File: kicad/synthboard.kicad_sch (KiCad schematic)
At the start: 11 parts, among them J1 Conn_02x20_Odd_Even, J2 Conn_02x20_Odd_Even, J3 Analog_Audio_Out, U1 MAX98357A

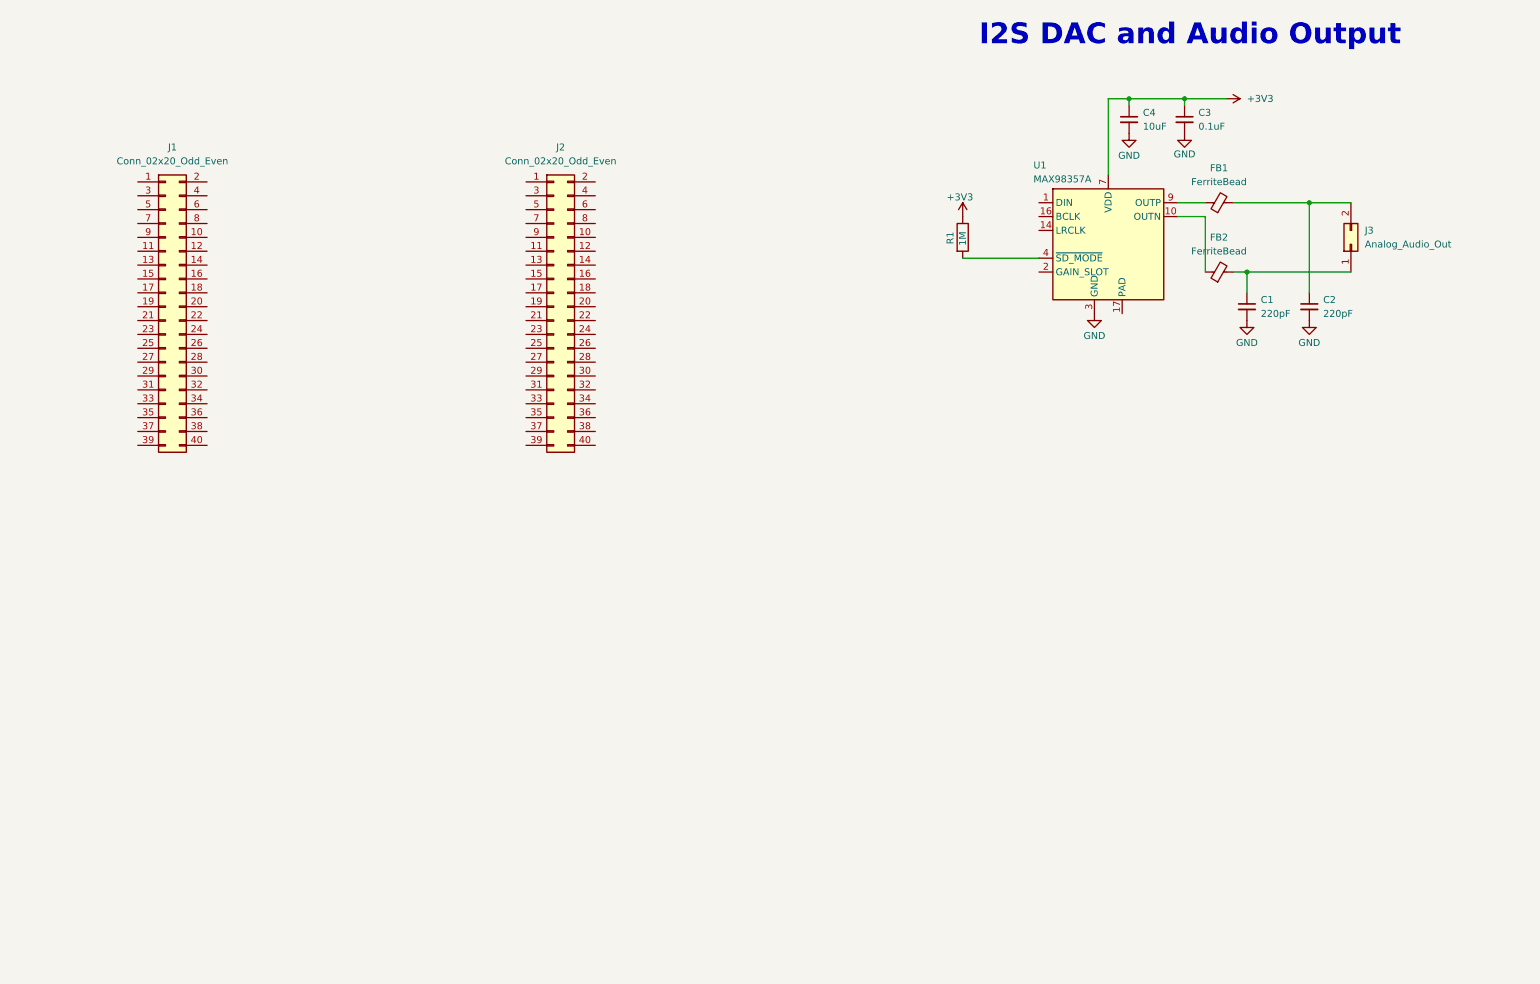
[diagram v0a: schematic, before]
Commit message: PCB development for input board started
Not done. Need to make a GND and +3.3V layer
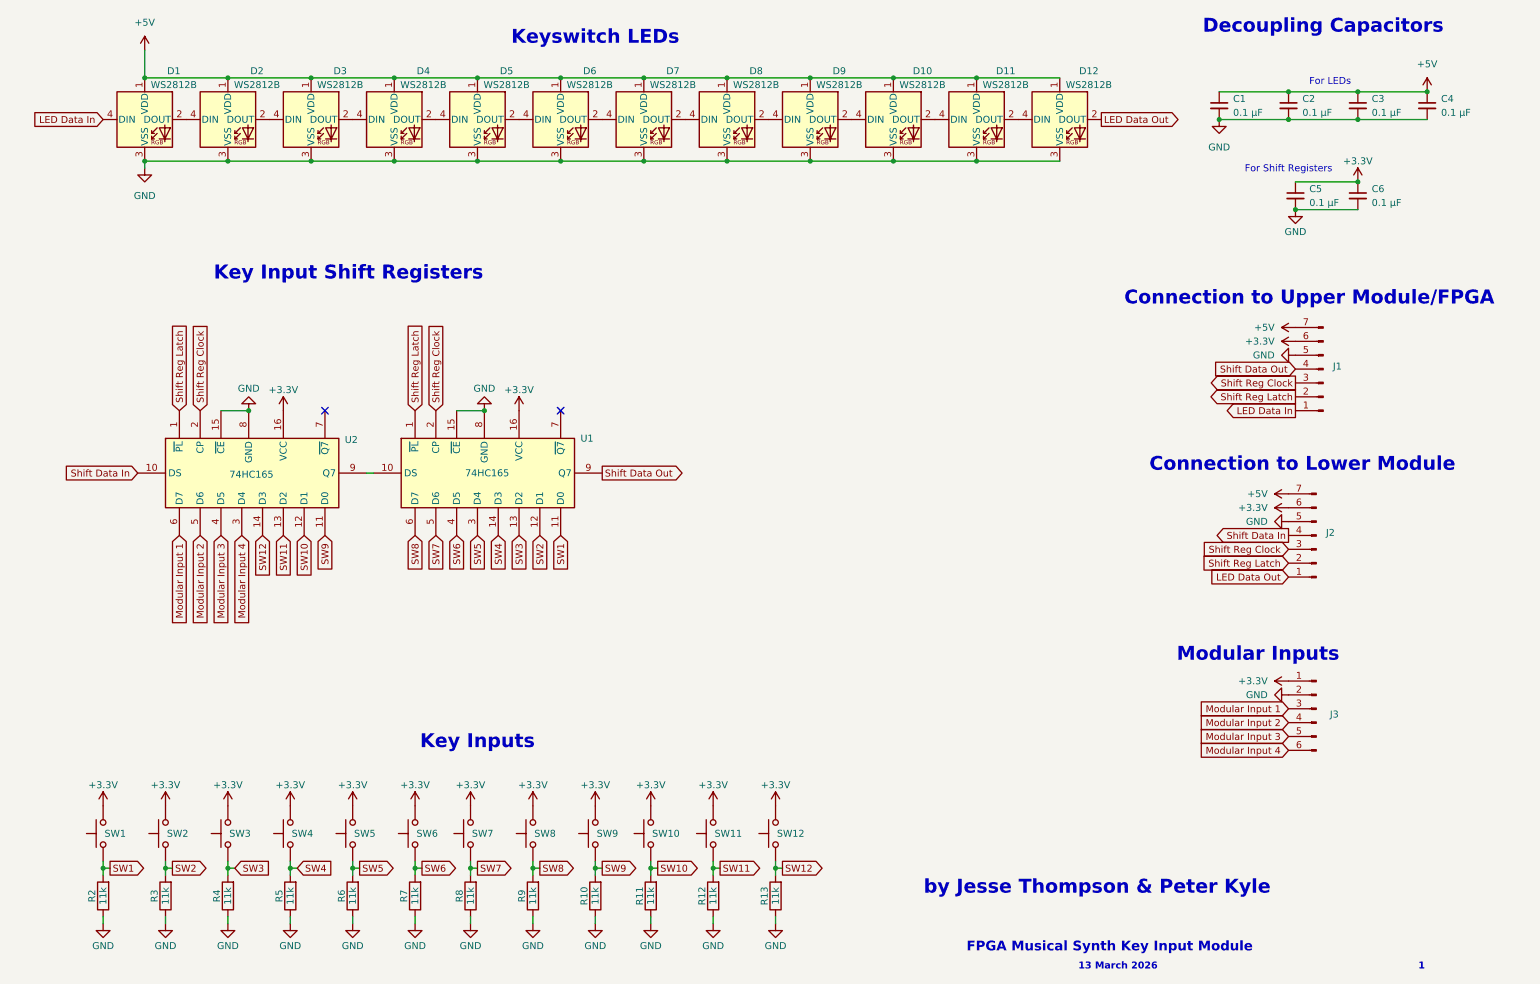
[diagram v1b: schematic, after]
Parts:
- removed FB1, FB2: FerriteBead, symbol Device:FerriteBead_Small
- removed J1, J2: Conn_02x20_Odd_Even, symbol Connector_Generic:Conn_02x20_Odd_Even
- removed J3: Analog_Audio_Out, symbol Connector_Generic:Conn_02x01
- removed R1: 1M, symbol Device:R
- removed U1: MAX98357A, Package_DFN_QFN:TQFN-16-1EP_3x3mm_P0.5mm_EP1.23x1.23mm, symbol Audio:MAX98357A
- added C5, C6: 0.1 µF, Capacitor_SMD:C_0805_2012Metric, symbol Device:C_Small
- added D1, D10, D11, D12, D2, D3, D4, D5, D6, D7, D8, D9: WS2812B, LED_SMD:LED_WS2812B_PLCC4_5.0x5.0mm_P3.2mm, symbol LED:WS2812B
- added J1: Connection to Upper Module/FPGA, Connector_PinHeader_2.54mm:PinHeader_1x07_P2.54mm_Vertical, symbol Connector:Conn_01x07_Pin
- added J2: Connection to Lower Module, Connector_PinHeader_2.54mm:PinHeader_1x07_P2.54mm_Vertical, symbol Connector:Conn_01x07_Pin
- added J3: Modular Inputs, Connector_PinHeader_2.54mm:PinHeader_1x06_P2.54mm_Vertical, symbol Connector:Conn_01x06_Pin
- added R10, R11, R12, R13, R2, R3, R4, R5, R6, R7, R8, R9: 11k, Resistor_SMD:R_0805_2012Metric, symbol Device:R
- added SW1, SW10, SW11, SW12, SW2, SW3, SW4, SW5, SW6, SW7, SW8, SW9: SW_Push, Button_Switch_Keyboard:SW_Cherry_MX_1.00u_Plate, symbol Switch:SW_Push
- added U1, U2: 74HC165, 74HC165D_653:SOIC127P600X175-16N, symbol 74xx:74HC165
- C1, C2: value 220pF -> 0.1 µF; footprint (none) -> Capacitor_SMD:C_0805_2012Metric
- C3: value 0.1uF -> 0.1 µF; footprint (none) -> Capacitor_SMD:C_0805_2012Metric
- C4: value 10uF -> 0.1 µF; footprint (none) -> Capacitor_SMD:C_0805_2012Metric
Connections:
- net +3V3 is gone; now on net +5V: C3.1, C4.1
- net GND: now also C5.2, C6.2, D1.3 (VSS), D10.3 (VSS), D11.3 (VSS), D12.3 (VSS), D2.3 (VSS), D3.3 (VSS), D4.3 (VSS), D5.3 (VSS), D6.3 (VSS), D7.3 (VSS), D8.3 (VSS), D9.3 (VSS), J1.5 (Pin_5), J2.5 (Pin_5), J3.2 (Pin_2), R10.1, R11.1, R12.1, R13.1, R2.1, R3.1, R4.1, R5.1, R6.1, R7.1, R8.1, R9.1, U1.15 (~{CE}), U1.8 (GND), U2.15 (~{CE}), U2.8 (GND)
- net +5V: now reaches C2.1
- net +5V: now also C1.1, D1.1 (VDD), D10.1 (VDD), D11.1 (VDD), D12.1 (VDD), D2.1 (VDD), D3.1 (VDD), D4.1 (VDD), D5.1 (VDD), D6.1 (VDD), D7.1 (VDD), D8.1 (VDD), D9.1 (VDD), J1.7 (Pin_7), J2.7 (Pin_7)
- new net: D10.2 (DOUT), D11.4 (DIN)
- new net: D10.4 (DIN), D9.2 (DOUT)
- new net: D11.2 (DOUT), D12.4 (DIN)
- new net: D6.2 (DOUT), D7.4 (DIN)
- new net: D5.2 (DOUT), D6.4 (DIN)
- new net: U1.10 (DS), U2.9 (Q7)
- new net: D2.2 (DOUT), D3.4 (DIN)
- new net: D1.2 (DOUT), D2.4 (DIN)
- new net: D7.2 (DOUT), D8.4 (DIN)
- new net: D4.2 (DOUT), D5.4 (DIN)
- new net: D3.2 (DOUT), D4.4 (DIN)
- new net: D8.2 (DOUT), D9.4 (DIN)
- new net +3.3V: C5.1, C6.1, J1.6 (Pin_6), J2.6 (Pin_6), J3.1 (Pin_1), SW1.2, SW10.2, SW11.2, SW12.2, SW2.2, SW3.2, SW4.2, SW5.2, SW6.2, SW7.2, SW8.2, SW9.2, U1.16 (VCC), U2.16 (VCC)
- new net LED Data In: D1.4 (DIN), J1.1 (Pin_1)
- new net LED Data Out: D12.2 (DOUT), J2.1 (Pin_1)
- new net Modular Input 1: J3.3 (Pin_3), U2.6 (D7)
- new net Modular Input 2: J3.4 (Pin_4), U2.5 (D6)
- new net Modular Input 3: J3.5 (Pin_5), U2.4 (D5)
- new net Modular Input 4: J3.6 (Pin_6), U2.3 (D4)
- new net SW1: R2.2, SW1.1, U1.11 (D0)
- new net SW10: R11.2, SW10.1, U2.12 (D1)
- new net SW11: R12.2, SW11.1, U2.13 (D2)
- new net SW12: R13.2, SW12.1, U2.14 (D3)
- new net SW2: R3.2, SW2.1, U1.12 (D1)
- new net SW3: R4.2, SW3.1, U1.13 (D2)
- new net SW4: R5.2, SW4.1, U1.14 (D3)
- new net SW5: R6.2, SW5.1, U1.3 (D4)
- new net SW6: R7.2, SW6.1, U1.4 (D5)
- new net SW7: R8.2, SW7.1, U1.5 (D6)
- new net SW8: R9.2, SW8.1, U1.6 (D7)
- new net SW9: R10.2, SW9.1, U2.11 (D0)
- new net Shift Data In: J2.4 (Pin_4), U2.10 (DS)
- new net Shift Data Out: J1.4 (Pin_4), U1.9 (Q7)
- new net Shift Reg Clock: J1.3 (Pin_3), J2.3 (Pin_3), U1.2 (CP), U2.2 (CP)
- new net Shift Reg Latch: J1.2 (Pin_2), J2.2 (Pin_2), U1.1 (~{PL}), U2.1 (~{PL})
- no-connect marks 0 -> 2
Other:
- note added: "1"
- note added: "13 March 2026"
- note added: "Connection to Lower Module"
- note added: "Connection to Upper Module/FPGA"
- note added: "Decoupling Capacitors"
- note added: "FPGA Musical Synth Key Input Module"
- note added: "For LEDs"
- note added: "For Shift Registers"
- note added: "Key Input Shift Registers"
- note added: "Key Inputs"
- note added: "Keyswitch LEDs"
- note added: "Modular Inputs"
- note added: "by Jesse Thompson & Peter Kyle"
- note removed: "I2S DAC and Audio Output"
